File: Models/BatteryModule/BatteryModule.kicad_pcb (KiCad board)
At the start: 2 copper layers, 0 parts

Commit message: Setting up the battery module PCB
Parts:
- added J1: Conn_01x02_Pin, Connector_Custom:PinHeader_1x2, B.Cu at (65.3, 74.2)
- added J2: Conn_01x02_Pin, Connector_Custom:PinHeader_1x2, B.Cu at (74.7, 74.2)
- added J3: Keystone_968, Connector_Custom:Keystone_968, F.Cu at (128.6, 86.3)
- added J4: Keystone_968, Connector_Custom:Keystone_968, F.Cu at (138.5, 120.2)
- added J5: Keystone_968, Connector_Custom:Keystone_968, F.Cu at (171.0, 90.2)
- added J6: Keystone_968, Connector_Custom:Keystone_968, F.Cu at (189.1, 123.6)
- added J7: Conn_01x02_Pin, Connector_Custom:PinHeader_1x2, B.Cu at (85.5, 74.3)
- added J8: Conn_01x02_Pin, Connector_Custom:PinHeader_1x2, B.Cu at (97.0, 74.3)
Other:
- board text added: "TODO: Hide all reference designators from the silkscreen layer after positioning components."

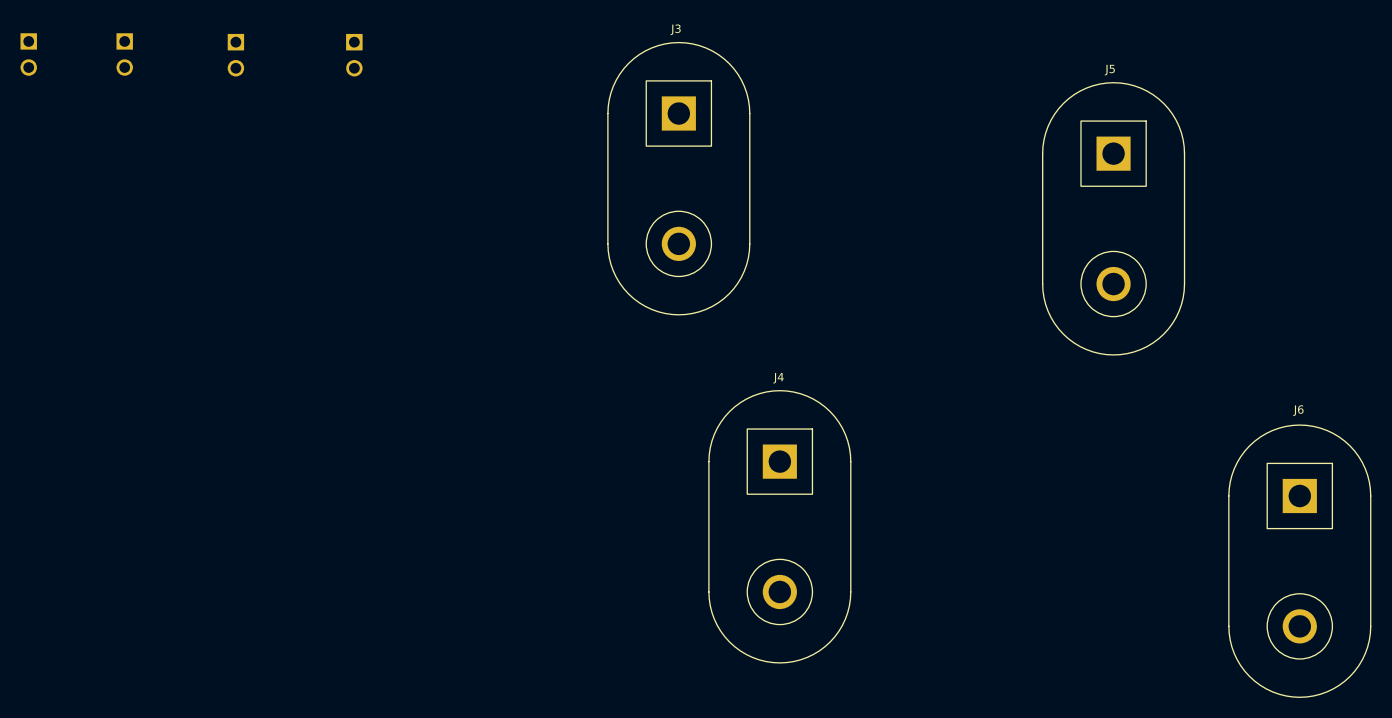
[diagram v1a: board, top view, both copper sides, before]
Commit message: Aligned the text artwork for one battery, three left to go
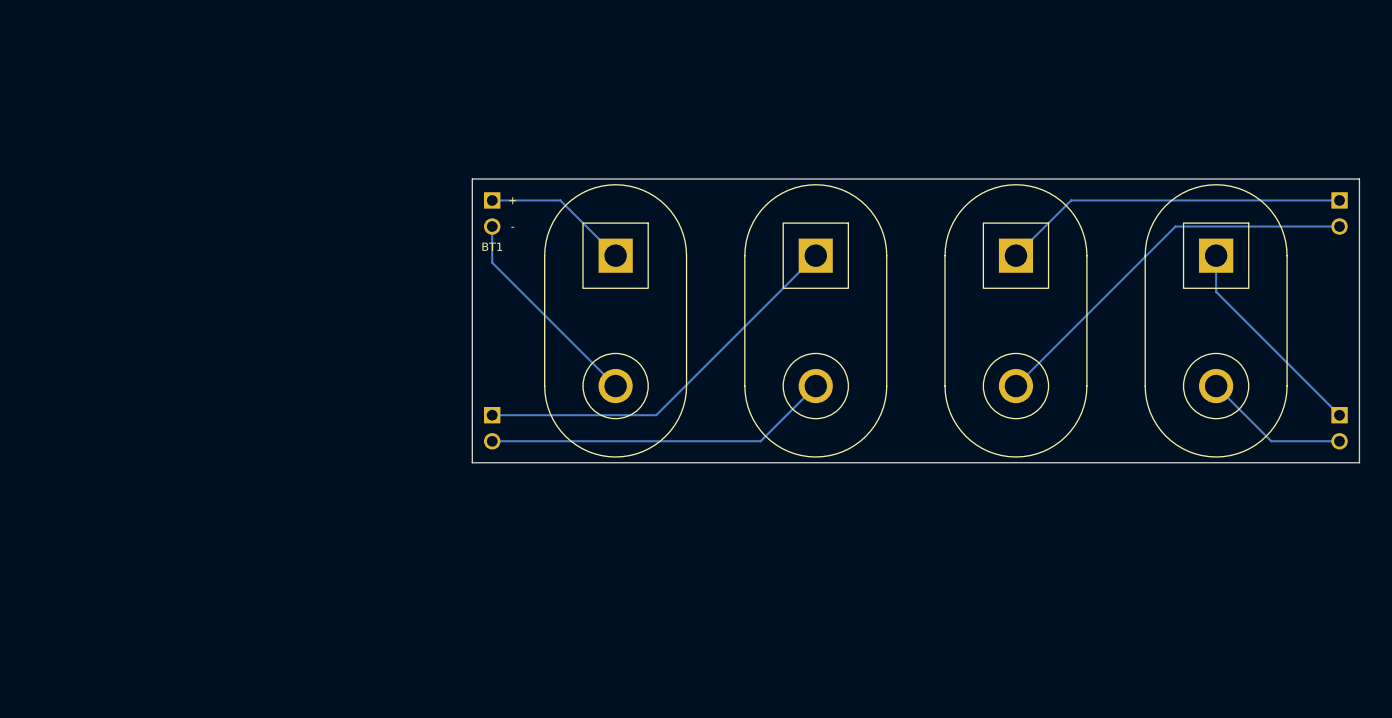
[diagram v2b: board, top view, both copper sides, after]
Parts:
- moved J7 108.6 mm to (193.0, 89.7)
- moved J8 102.6 mm to (193.0, 110.6)
- moved J2 51.1 mm to (110.5, 110.6)
- moved J1 47.7 mm to (110.5, 89.7)
- moved J6 24.8 mm to (181.0, 100.2)
- moved J4 20.4 mm to (142.0, 100.2)
- moved J3 15.2 mm to (122.5, 100.2)
- moved J5 13.8 mm to (161.5, 100.2)
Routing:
- net Net-(J5--): track 0.00 -> 38.0 mm
- net Net-(J2-Pin_1): track 0.00 -> 38.0 mm
- net Net-(J5-+): track 0.00 -> 33.7 mm
- net Net-(J2-Pin_2): track 0.00 -> 33.7 mm
- net Net-(J1-Pin_2): track 0.00 -> 20.5 mm
- net Net-(J6-+): track 0.00 -> 20.5 mm
- net Net-(J1-Pin_1): track 0.00 -> 14.2 mm
- net Net-(J6--): track 0.00 -> 14.2 mm
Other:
- board outline added: 86.4 x 27.6 mm
- board text added: "+"
- board text added: "-"
- board text added: "BT1"
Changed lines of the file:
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@@
 	(net 8 "Net-(J6-+)")
 	(footprint "Connector_Custom:Keystone_968"
+		(locked yes)
 		(layer "F.Cu")
-		(at 128.64 86.31 -90)
+		(at 122.48 100.16 -90)
 		(property "Reference" "J3"
 			(at -14.58 0.24 0)
 			(unlocked yes)
 			(layer "F.SilkS")
+			(hide yes)
 			(effects
 				(font
@@
 	)
 	(footprint "Connector_Custom:Keystone_968"
+		(locked yes)
 		(layer "F.Cu")
-		(at 189.13 123.57 -90)
+		(at 180.98 100.16 -90)
 		(property "Reference" "J6"
-			(at -14.74 0.07 0)
-			(unlocked yes)
-			(layer "F.SilkS")
+			(at -14.55 0.18 0)
+			(unlocked yes)
+			(layer "F.SilkS")
+			(hide yes)
 			(effects
 				(font
@@
 	)
 	(footprint "Connector_Custom:Keystone_968"
+		(locked yes)
 		(layer "F.Cu")
-		(at 138.48 120.22 -90)
+		(at 141.98 100.16 -90)
 		(property "Reference" "J4"
 			(at -14.55 0.07 0)
 			(unlocked yes)
 			(layer "F.SilkS")
+			(hide yes)
 			(effects
 				(font
@@
 	)
 	(footprint "Connector_Custom:Keystone_968"
+		(locked yes)
 		(layer "F.Cu")
-		(at 170.99 90.22 -90)
+		(at 161.48 100.16 -90)
 		(property "Reference" "J5"
 			(at -14.57 0.29 0)
 			(unlocked yes)
 			(layer "F.SilkS")
+			(hide yes)
 			(effects
 				(font
@@
 	)
 	(footprint "Connector_Custom:PinHeader_1x2"
-		(layer "B.Cu")
-		(at 85.49 74.28 180)
+		(locked yes)
+		(layer "B.Cu")
+		(at 193 89.7 180)
 		(property "Reference" "J7"
 			(at 0.04 3.67 0)
 			(unlocked yes)
 			(layer "B.SilkS")
+			(hide yes)
 			(effects
 				(font
@@
 	)
 	(footprint "Connector_Custom:PinHeader_1x2"
-		(layer "B.Cu")
-		(at 74.66 74.21 180)
+		(locked yes)
+		(layer "B.Cu")
+		(at 110.46 110.62 180)
 		(property "Reference" "J2"
 			(at 0.08 3.76 0)
 			(unlocked yes)
 			(layer "B.SilkS")
+			(hide yes)
 			(effects
 				(font
@@
 	)
 	(footprint "Connector_Custom:PinHeader_1x2"
-		(layer "B.Cu")
-		(at 97.03 74.28 180)
+		(locked yes)
+		(layer "B.Cu")
+		(at 193 110.62 180)
 		(property "Reference" "J8"
 			(at 0.05 3.6 0)
 			(unlocked yes)
 			(layer "B.SilkS")
+			(hide yes)
 			(effects
 				(font
@@
 	)
 	(footprint "Connector_Custom:PinHeader_1x2"
-		(layer "B.Cu")
-		(at 65.31 74.21 180)
+		(locked yes)
+		(layer "B.Cu")
+		(at 110.46 89.7 180)
 		(property "Reference" "J1"
 			(at 0.07 3.78 0)
 			(unlocked yes)
 			(layer "B.SilkS")
+			(hide yes)
 			(effects
 				(font
@@
 		(embedded_fonts no)
 	)
+	(gr_rect
+		(start 108.52 86.34)
+		(end 194.94 113.98)
+		(stroke
+			(width 0.05)
+			(type default)
+		)
+		(fill no)
+		(layer "Edge.Cuts")
+	)
+	(gr_text "BT1"
+		(at 110.46 92.97 0)
+		(layer "F.SilkS")
+		(effects
+			(font
+				(size 0.8 0.8)
+				(thickness 0.12)
+			)
+		)
+	)
+	(gr_text "-"
+		(at 112.46 90.97 0)
+		(layer "F.SilkS")
+		(effects
+			(font
+				(size 0.8 0.8)
+				(thickness 0.12)
+			)
+		)
+	)
+	(gr_text "+"
+		(at 112.46 88.43 0)
+		(layer "F.SilkS")
+		(effects
+			(font
+				(size 0.8 0.8)
+				(thickness 0.12)
+			)
+		)
+	)
 	(gr_text "TODO: Hide all reference designators from the\nsilkscreen layer after positioning components."
 		(at 104.79 46.36 0)
@@
 		)
 	)
+	(segment
+		(start 117.1 88.43)
+		(end 122.48 93.81)
+		(width 0.2)
+		(layer "B.Cu")
+		(net 1)
+	)
+	(segment
+		(start 110.46 88.43)
+		(end 117.1 88.43)
+		(width 0.2)
+		(layer "B.Cu")
+		(net 1)
+	)
+	(segment
+		(start 110.46 94.49)
+		(end 110.46 90.97)
+		(width 0.2)
+		(layer "B.Cu")
+		(net 2)
+	)
+	(segment
+		(start 122.48 106.51)
+		(end 110.46 94.49)
+		(width 0.2)
+		(layer "B.Cu")
+		(net 2)
+	)
+	(segment
+		(start 126.44 109.35)
+		(end 110.46 109.35)
+		(width 0.2)
+		(layer "B.Cu")
+		(net 3)
+	)
+	(segment
+		(start 141.98 93.81)
+		(end 126.44 109.35)
+		(width 0.2)
+		(layer "B.Cu")
+		(net 3)
+	)
+	(segment
+		(start 136.6 111.89)
+		(end 110.46 111.89)
+		(width 0.2)
+		(layer "B.Cu")
+		(net 4)
+	)
+	(segment
+		(start 141.98 106.51)
+		(end 136.6 111.89)
+		(width 0.2)
+		(layer "B.Cu")
+		(net 4)
+	)
+	(segment
+		(start 166.86 88.43)
+		(end 193 88.43)
+		(width 0.2)
+		(layer "B.Cu")
+		(net 5)
+	)
+	(segment
+		(start 161.48 93.81)
+		(end 166.86 88.43)
+		(width 0.2)
+		(layer "B.Cu")
+		(net 5)
+	)
+	(segment
+		(start 161.48 106.51)
+		(end 177.02 90.97)
+		(width 0.2)
+		(layer "B.Cu")
+		(net 6)
+	)
+	(segment
+		(start 177.02 90.97)
+		(end 193 90.97)
+		(width 0.2)
+		(layer "B.Cu")
+		(net 6)
+	)
+	(segment
+		(start 180.98 106.51)
+		(end 186.36 111.89)
+		(width 0.2)
+		(layer "B.Cu")
+		(net 7)
+	)
+	(segment
+		(start 186.36 111.89)
+		(end 193 111.89)
+		(width 0.2)
+		(layer "B.Cu")
+		(net 7)
+	)
+	(segment
+		(start 180.98 97.33)
+		(end 193 109.35)
+		(width 0.2)
+		(layer "B.Cu")
+		(net 8)
+	)
+	(segment
+		(start 180.98 93.81)
+		(end 180.98 97.33)
+		(width 0.2)
+		(layer "B.Cu")
+		(net 8)
+	)
 	(embedded_fonts no)

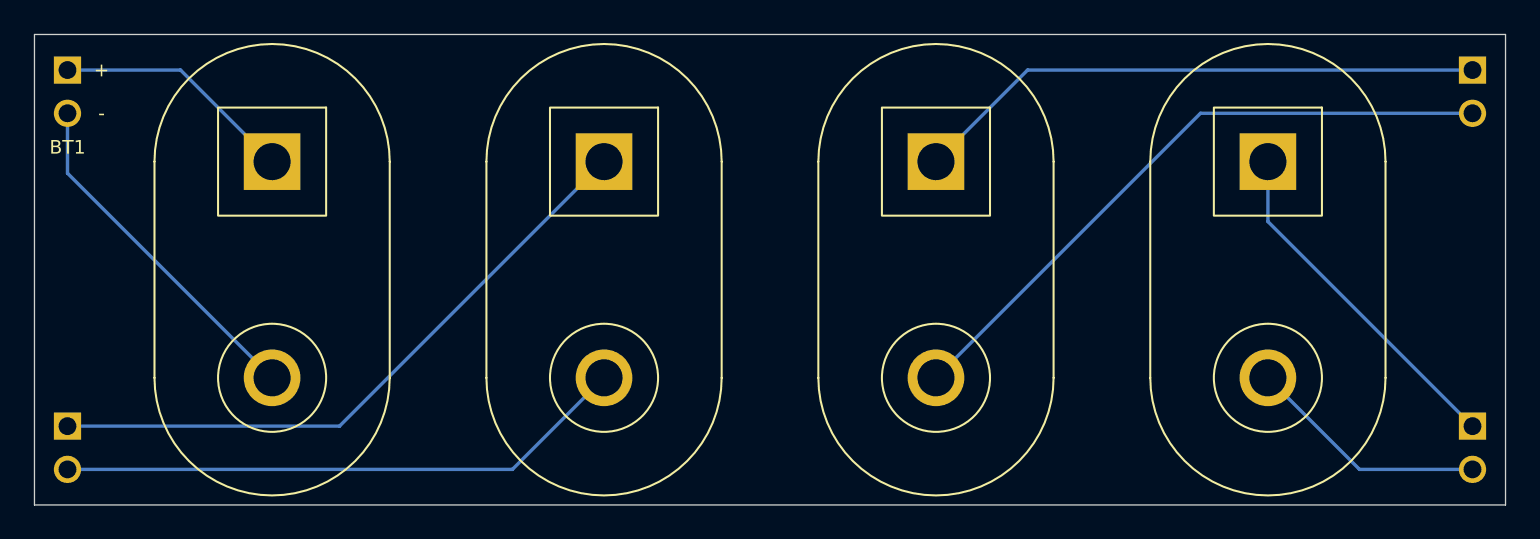
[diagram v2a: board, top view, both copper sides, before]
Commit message: Finished the PCB for the battery holder
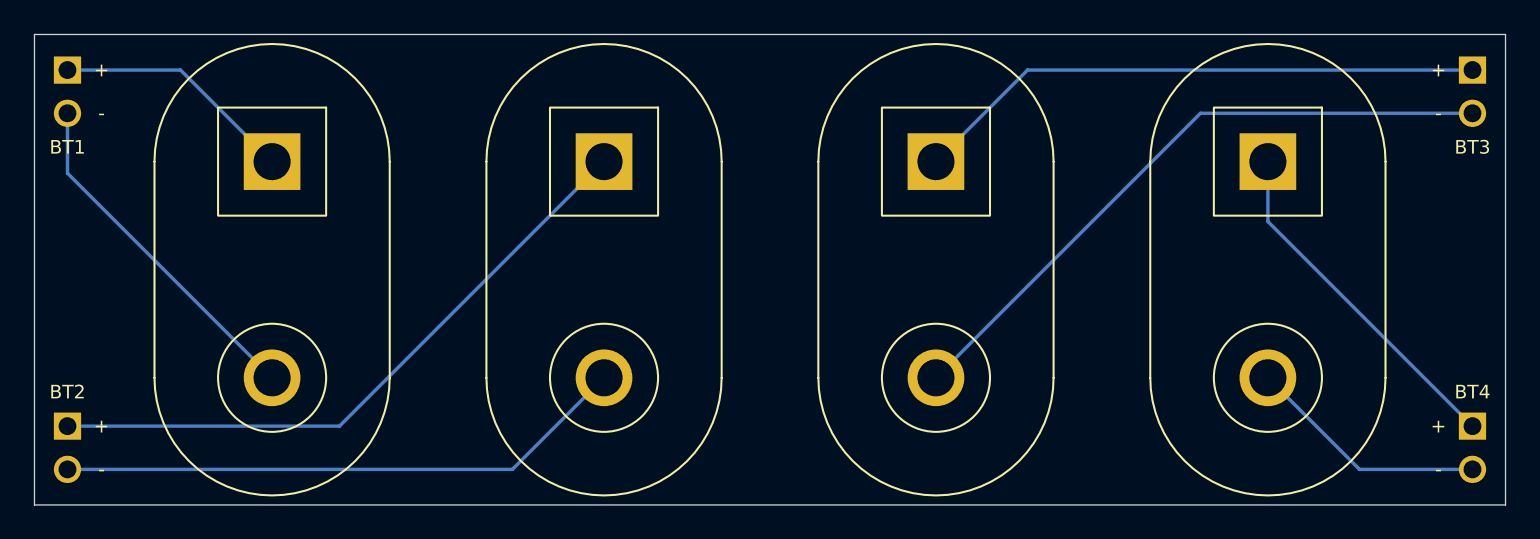
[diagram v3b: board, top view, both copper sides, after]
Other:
- board text added: "BT2"
- board text added: "BT3"
- board text added: "BT4"
- board text removed: "TODO: Hide all reference designators from the silkscreen layer after positioning components."
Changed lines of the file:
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@@
+		)
+	)
+	(gr_text "+"
+		(at 191 109.35 0)
+		(layer "F.SilkS")
+		(effects
+			(font
+				(size 0.8 0.8)
+				(thickness 0.12)
+			)
+		)
+	)
+	(gr_text "BT2"
+		(at 110.46 107.35 0)
+		(layer "F.SilkS")
+		(effects
+			(font
+				(size 0.8 0.8)
+				(thickness 0.12)
+			)
+		)
+	)
+	(gr_text "BT3"
+		(at 193 92.97 0)
+		(layer "F.SilkS")
+		(effects
+			(font
+				(size 0.8 0.8)
+				(thickness 0.12)
+			)
+		)
+	)
+	(gr_text "-"
+		(at 191 90.97 0)
+		(layer "F.SilkS")
+		(effects
+			(font
+				(size 0.8 0.8)
+				(thickness 0.12)
+			)
+		)
+	)
+	(gr_text "-"
+		(at 191 111.89 0)
+		(layer "F.SilkS")
+		(effects
+			(font
+				(size 0.8 0.8)
+				(thickness 0.12)
+			)
 		)
 	)
 	(gr_text "-"
 		(at 112.46 90.97 0)
+		(layer "F.SilkS")
+		(effects
+			(font
+				(size 0.8 0.8)
+				(thickness 0.12)
+			)
+		)
+	)
+	(gr_text "-"
+		(at 112.46 111.89 0)
+		(layer "F.SilkS")
+		(effects
+			(font
+				(size 0.8 0.8)
+				(thickness 0.12)
+			)
+		)
+	)
+	(gr_text "BT4"
+		(at 193 107.35 0)
+		(layer "F.SilkS")
+		(effects
+			(font
+				(size 0.8 0.8)
+				(thickness 0.12)
+			)
+		)
+	)
+	(gr_text "+"
+		(at 191 88.43 0)
+		(layer "F.SilkS")
+		(effects
+			(font
+				(size 0.8 0.8)
+				(thickness 0.12)
+			)
+		)
+	)
+	(gr_text "+"
+		(at 112.46 109.35 0)
 		(layer "F.SilkS")
 		(effects
@@
 		)
 	)
-	(gr_text "TODO: Hide all reference designators from the\nsilkscreen layer after positioning components."
-		(at 104.79 46.36 0)
-		(layer "User.2")
-		(effects
-			(font
-				(size 1.5 1.5)
-				(thickness 0.3)
-				(bold yes)
-			)
-			(justify left top)
-		)
-	)
